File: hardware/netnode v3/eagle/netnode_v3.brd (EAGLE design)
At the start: 59.9 x 58.9 mm, 25 parts, among them IC1 TSR-1, IC2 PIC18F4K80, X1 DC10R, X2 XPORT

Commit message: Pre-final board files, silkscreen to be fixed
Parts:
- removed C5: 100n, rcl:C0603
- removed JP1: (no value), pinhead:1X06
- removed RST: 9902031, netnode:PUSHBUTTON
- removed UART: (no value), pinhead:1X04
- added ANALOG: (no value), pinhead:1X06
- added IC3: FOD060L, ic:SO-08
- added R1: 2K, rcl:R0603
- added R2: (no value), rcl:M0805
- added UART2: (no value), pinhead:1X04
- moved IO1 52.2 mm to (8.89, 5.08), turned to 0 degrees
- moved IO2 49.5 mm to (52.1, 5.08)
- moved X1 45.6 mm to (6.35, 53.3), turned to 270 degrees
- moved X2 38.8 mm to (16.5, 53.3), turned to 270 degrees
- moved SUP 36.1 mm to (2.54, 39.4), turned to 270 degrees
- moved HBEAT 24.3 mm to (14.0, 10.2), turned to 270 degrees
- moved XPORT 20.1 mm to (14.0, 14.0), turned to 270 degrees
- moved IC1 19.4 mm to (5.08, 26.7), turned to 0 degrees
- moved C1 19.1 mm to (13.8, 37.1), turned to 180 degrees
- moved C6 19.1 mm to (49.5, 38.1), turned to 0 degrees
- moved RN3 18.3 mm to (10.5, 22.9), turned to 0 degrees
- moved C7 18.2 mm to (34.3, 38.1), turned to 270 degrees
- moved PWR 17.3 mm to (14.0, 17.8), turned to 270 degrees
- moved RN1 16.2 mm to (44.5, 12.7)
- moved C2 15.9 mm to (13.8, 33.8), turned to 180 degrees
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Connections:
- removed net N$12: IC2.2, UART.2
- removed net N$9: HBEAT.C, IC2.15
- new net HBEAT: HBEAT.C, IC2.40
- new net N$3: IO1.1, R2.2
- new net OPTO1: IC2.41, IC3.6, R1.1
- new net RD4: IC2.2, UART2.2
- net !MCLR: no longer RST.3
- net +3V3: now also IC3.8, IO1.8, IO2.5, IO2.6, R1.2, RN3.6; no longer C5.1, IO1.1, RN3.5
- net AN0: now also ANALOG.1; no longer JP1.1
- net AN1: now also ANALOG.2; no longer JP1.2
- net AN2: now also ANALOG.4; no longer JP1.4
- net AN3: now also ANALOG.5; no longer JP1.5
- net GND: now also ANALOG.3, ANALOG.6, IC3.5, IO1.7, IO2.7, UART2.1; no longer C5.2, IO1.2, IO2.2, IO2.4, IO2.6, JP1.3, JP1.6, RST.1, UART.1
- net IN0: now also IO2.4, RN1.5; no longer IO2.1, RN1.8
- net IN1: now also RN1.6; no longer RN1.7
- net IN2: now also IO2.2, RN1.7; no longer IO2.5, RN1.6
- net IN3: now also IO2.1, RN1.8; no longer IO2.7, RN1.5
- net N$2: now also RN3.3; no longer RN3.1
- net N$8: now also RN3.1; no longer RN3.4
- net OPTO+: now also IC3.2, R2.1; no longer IO1.5
- net OPTO-: now also IC3.3, IO1.2; no longer IO1.6
- net OW: now also IO1.5; no longer IO1.7
- net PIC_RTS: now also IC2.35
- net PWM: now also IO1.6; no longer IO1.8
- net RX2: now also UART2.4; no longer UART.4
- net TX2: now also UART2.3; no longer UART.3
- net XPORT_RST: now also IC2.36
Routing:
- net +3V3: track 11.9 -> 241.2 mm, vias 0 -> 4
- net OPTO1: track 0.00 -> 59.2 mm, vias 0 -> 2
- net HBEAT: track 0.00 -> 45.5 mm, vias 0 -> 2
- net SCL: track 0.00 -> 41.0 mm, vias 0 -> 1
- net OW: track 0.00 -> 40.1 mm, vias 0 -> 1
- net SDA: track 0.00 -> 38.6 mm, vias 0 -> 1
- net PWM: track 0.00 -> 33.5 mm, vias 0 -> 1
- net XPORT_STAT: track 0.00 -> 32.1 mm, vias 0 -> 2
- net IN3: track 0.00 -> 27.8 mm, vias 0 -> 2
- net IN0: track 0.00 -> 26.8 mm, vias 0 -> 2
- net XPORT_RST: track 0.00 -> 25.5 mm, vias 0 -> 1
- net IN2: track 0.00 -> 23.8 mm, vias 0 -> 2
- net IN1: track 0.00 -> 22.5 mm
- net VSUPPLY: track 0.00 -> 21.5 mm
- net AN0: track 0.00 -> 20.1 mm, vias 0 -> 1
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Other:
- board size 59.9 x 58.9 mm -> 59.9 x 49.9 mm
- board text added: "0"
- board text added: "1"
- board text added: "2"
- board text added: "3"

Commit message: Further finalization of board
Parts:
- moved IO1 17.8 mm to (26.7, 5.08), turned to 180 degrees
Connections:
- net +3V3: now also IO1.1; no longer IO1.8
- net GND: now also IO1.2; no longer IO1.7
- net N$3: now also IO1.8; no longer IO1.1
- net OPTO-: now also IO1.7; no longer IO1.2
- net OW: now also IO1.4; no longer IO1.5
- net PWM: now also IO1.3; no longer IO1.6
- net SCL: now also IO1.6; no longer IO1.3
- net SDA: now also IO1.5; no longer IO1.4
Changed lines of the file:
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@@
 <setting verticaltext="up"/>
 </settings>
-<grid distance="1" unitdist="mm" unit="mm" style="lines" multiple="1" display="no" altdistance="0.127" altunitdist="mm" altunit="mm"/>
+<grid distance="2.54" unitdist="mm" unit="mm" style="lines" multiple="1" display="no" altdistance="0.127" altunitdist="mm" altunit="mm"/>
 <layers>
 <layer number="1" name="Top" color="4" fill="1" visible="yes" active="yes"/>
@@
 <layer number="27" name="tValues" color="7" fill="1" visible="no" active="yes"/>
 <layer number="28" name="bValues" color="7" fill="1" visible="no" active="yes"/>
-<layer number="29" name="tStop" color="7" fill="3" visible="yes" active="yes"/>
+<layer number="29" name="tStop" color="7" fill="3" visible="no" active="yes"/>
 <layer number="30" name="bStop" color="7" fill="6" visible="no" active="yes"/>
 <layer number="31" name="tCream" color="7" fill="4" visible="no" active="yes"/>
@@
 <attribute name="VALUE" x="14.639" y="36.066" size="1.27" layer="27" rot="R180"/>
 </element>
-<element name="IO1" library="netnode" package="SCREW_TERMINAL_8PINS" value="SCREW_TERMINAL" x="8.89" y="5.08">
-<attribute name="OC_FARNELL" value="3041438" x="8.89" y="5.08" size="1.778" layer="27" display="off"/>
-<attribute name="MF" value="PHOENIX CONTACT" x="8.89" y="5.08" size="1.778" layer="27" display="off"/>
-<attribute name="MPN" value="1725711" x="8.89" y="5.08" size="1.778" layer="27" display="off"/>
+<element name="IO1" library="netnode" package="SCREW_TERMINAL_8PINS" value="SCREW_TERMINAL" x="26.67" y="5.08" rot="R180">
+<attribute name="OC_FARNELL" value="3041438" x="26.67" y="5.08" size="1.778" layer="27" rot="R180" display="off"/>
+<attribute name="MF" value="PHOENIX CONTACT" x="26.67" y="5.08" size="1.778" layer="27" rot="R180" display="off"/>
+<attribute name="MPN" value="1725711" x="26.67" y="5.08" size="1.778" layer="27" rot="R180" display="off"/>
 </element>
 <element name="IO2" library="netnode" package="SCREW_TERMINAL_8PINS" value="SCREW_TERMINAL" x="52.07" y="5.08" rot="R180">
@@
 <contactref element="IC3" pad="5"/>
 <contactref element="IC3" pad="5"/>
-<contactref element="IO1" pad="7"/>
 <wire x1="44.12" y1="23.5" x2="44.12" y2="20.84" width="0.4064" layer="1"/>
 <wire x1="44.12" y1="20.84" x2="43.6" y2="20.32" width="0.4064" layer="1"/>
@@
 <via x="47.371" y="19.558" extent="1-16" drill="0.5"/>
 <via x="47.371" y="17.526" extent="1-16" drill="0.5"/>
+<contactref element="IO1" pad="2"/>
 </signal>
 <signal name="VSUPPLY" class="1">
@@
 <contactref element="IO2" pad="6"/>
 <contactref element="R1" pad="2"/>
-<contactref element="IO1" pad="8"/>
 <wire x1="44.92" y1="23.5" x2="44.92" y2="20.7" width="0.4064" layer="1"/>
 <wire x1="44.92" y1="20.7" x2="45.3" y2="20.32" width="0.4064" layer="1"/>
@@
 <wire x1="2.54" y1="10.16" x2="10.16" y2="2.54" width="1.016" layer="16" curve="90"/>
 <wire x1="10.16" y1="2.54" x2="26.67" y2="2.54" width="1.016" layer="16"/>
-<wire x1="26.67" y1="2.54" x2="39.37" y2="2.54" width="1.016" layer="16"/>
+<wire x1="27.94" y1="2.54" x2="39.37" y2="2.54" width="1.016" layer="16"/>
 <wire x1="39.37" y1="2.54" x2="41.91" y2="5.08" width="1.016" layer="16" curve="90"/>
 <wire x1="41.91" y1="5.08" x2="41.91" y2="9.84" width="0.4064" layer="1"/>
@@
 <wire x1="43.18" y1="7.62" x2="41.91" y2="6.35" width="0.4064" layer="16" curve="90"/>
 <wire x1="41.91" y1="6.35" x2="41.91" y2="5.08" width="0.4064" layer="16"/>
-<wire x1="26.67" y1="5.08" x2="26.67" y2="2.54" width="1.016" layer="16"/>
 <wire x1="39.37" y1="5.08" x2="41.91" y2="5.08" width="1.016" layer="16"/>
 <wire x1="55.746" y1="20.38" x2="55.94" y2="20.38" width="0.4064" layer="1"/>
@@
 <via x="40.64" y="41.91" extent="1-16" drill="0.5"/>
 <via x="41.91" y="41.91" extent="1-16" drill="0.5"/>
+<contactref element="IO1" pad="1"/>
+<wire x1="26.67" y1="5.08" x2="26.67" y2="2.54" width="1.016" layer="16"/>
+<wire x1="26.67" y1="2.54" x2="27.94" y2="2.54" width="1.016" layer="16"/>
 </signal>
 <signal name="XPORT_RST">
@@
 </signal>
 <signal name="SCL" class="1">
-<contactref element="IO1" pad="3"/>
 <contactref element="IC2" pad="37"/>
-<wire x1="13.97" y1="5.08" x2="13.97" y2="6.35" width="0.4064" layer="16"/>
 <wire x1="13.97" y1="6.35" x2="24.13" y2="16.51" width="0.4064" layer="16"/>
 <wire x1="24.13" y1="16.51" x2="31.75" y2="16.51" width="0.4064" layer="16"/>
@@
 <wire x1="33.02" y1="26.67" x2="37.25" y2="30.9" width="0.4064" layer="1"/>
 <wire x1="38.32" y1="30.9" x2="37.25" y2="30.9" width="0.4064" layer="1"/>
+<contactref element="IO1" pad="6"/>
+<wire x1="13.97" y1="6.35" x2="13.97" y2="5.08" width="0.4064" layer="16"/>
 </signal>
 <signal name="SDA" class="1">
-<contactref element="IO1" pad="4"/>
 <contactref element="IC2" pad="42"/>
-<wire x1="16.51" y1="5.08" x2="16.51" y2="6.35" width="0.4064" layer="16"/>
 <wire x1="16.51" y1="6.35" x2="24.13" y2="13.97" width="0.4064" layer="16"/>
 <wire x1="24.13" y1="13.97" x2="33.02" y2="13.97" width="0.4064" layer="16"/>
@@
 <wire x1="35.56" y1="20.32" x2="35.56" y2="16.51" width="0.4064" layer="16"/>
 <wire x1="35.56" y1="16.51" x2="33.02" y2="13.97" width="0.4064" layer="16"/>
+<contactref element="IO1" pad="5"/>
+<wire x1="16.51" y1="6.35" x2="16.51" y2="5.08" width="0.4064" layer="16"/>
 </signal>
 <signal name="OPTO+" class="1">
@@
 <signal name="OPTO-" class="1">
 <contactref element="IC3" pad="3"/>
-<contactref element="IO1" pad="2"/>
 <wire x1="5.715" y1="13.91" x2="5.715" y2="9.525" width="0.4064" layer="1"/>
 <wire x1="5.715" y1="9.525" x2="7.62" y2="7.62" width="0.4064" layer="1"/>
 <wire x1="7.62" y1="7.62" x2="10.16" y2="7.62" width="0.4064" layer="1"/>
 <wire x1="10.16" y1="7.62" x2="11.43" y2="6.35" width="0.4064" layer="1"/>
+<contactref element="IO1" pad="7"/>
 <wire x1="11.43" y1="6.35" x2="11.43" y2="5.08" width="0.4064" layer="1"/>
 </signal>
 <signal name="OW" class="1">
 <contactref element="IC2" pad="43"/>
-<contactref element="IO1" pad="5"/>
 <wire x1="38.32" y1="26.1" x2="40.64" y2="26.1" width="0.4064" layer="1"/>
 <wire x1="40.64" y1="26.1" x2="40.64" y2="26.67" width="0.4064" layer="1"/>
@@
 <wire x1="35.56" y1="11.43" x2="24.13" y2="11.43" width="0.4064" layer="16"/>
 <wire x1="24.13" y1="11.43" x2="19.05" y2="6.35" width="0.4064" layer="16"/>
+<contactref element="IO1" pad="4"/>
 <wire x1="19.05" y1="6.35" x2="19.05" y2="5.08" width="0.4064" layer="16"/>
 </signal>
 <signal name="PWM" class="1">
 <contactref element="IC2" pad="3"/>
-<contactref element="IO1" pad="6"/>
 <wire x1="41.72" y1="23.5" x2="41.72" y2="21.4" width="0.4064" layer="1"/>
 <wire x1="41.72" y1="21.4" x2="40.64" y2="20.32" width="0.4064" layer="1"/>
@@
 <wire x1="35.56" y1="8.89" x2="24.13" y2="8.89" width="0.4064" layer="16"/>
 <wire x1="24.13" y1="8.89" x2="21.59" y2="6.35" width="0.4064" layer="16"/>
+<contactref element="IO1" pad="3"/>
 <wire x1="21.59" y1="6.35" x2="21.59" y2="5.08" width="0.4064" layer="16"/>
 </signal>
@@
 <via x="19.05" y="16.51" extent="1-16" drill="0.5"/>
 </signal>
-<signal name="N$3">
-<contactref element="IO1" pad="1"/>
-<contactref element="R2" pad="2"/>
-<wire x1="8.89" y1="5.08" x2="5.08" y2="5.08" width="0.4064" layer="1"/>
-<wire x1="5.08" y1="5.08" x2="3.81" y2="6.35" width="0.4064" layer="1"/>
-<wire x1="3.81" y1="6.35" x2="3.81" y2="6.67" width="0.4064" layer="1"/>
-</signal>
 <signal name="N$2">
 <contactref element="PWR" pad="A"/>
@@
 <wire x1="11.43" y1="17.78" x2="12.22" y2="17.78" width="0.4064" layer="1"/>
 </signal>
+<signal name="N$3">
+<contactref element="IO1" pad="8"/>
+<contactref element="R2" pad="2"/>
+<wire x1="3.81" y1="6.67" x2="5.4" y2="5.08" width="0.4064" layer="1" curve="90"/>
+<wire x1="5.4" y1="5.08" x2="8.89" y2="5.08" width="0.4064" layer="1"/>
+</signal>
 </signals>

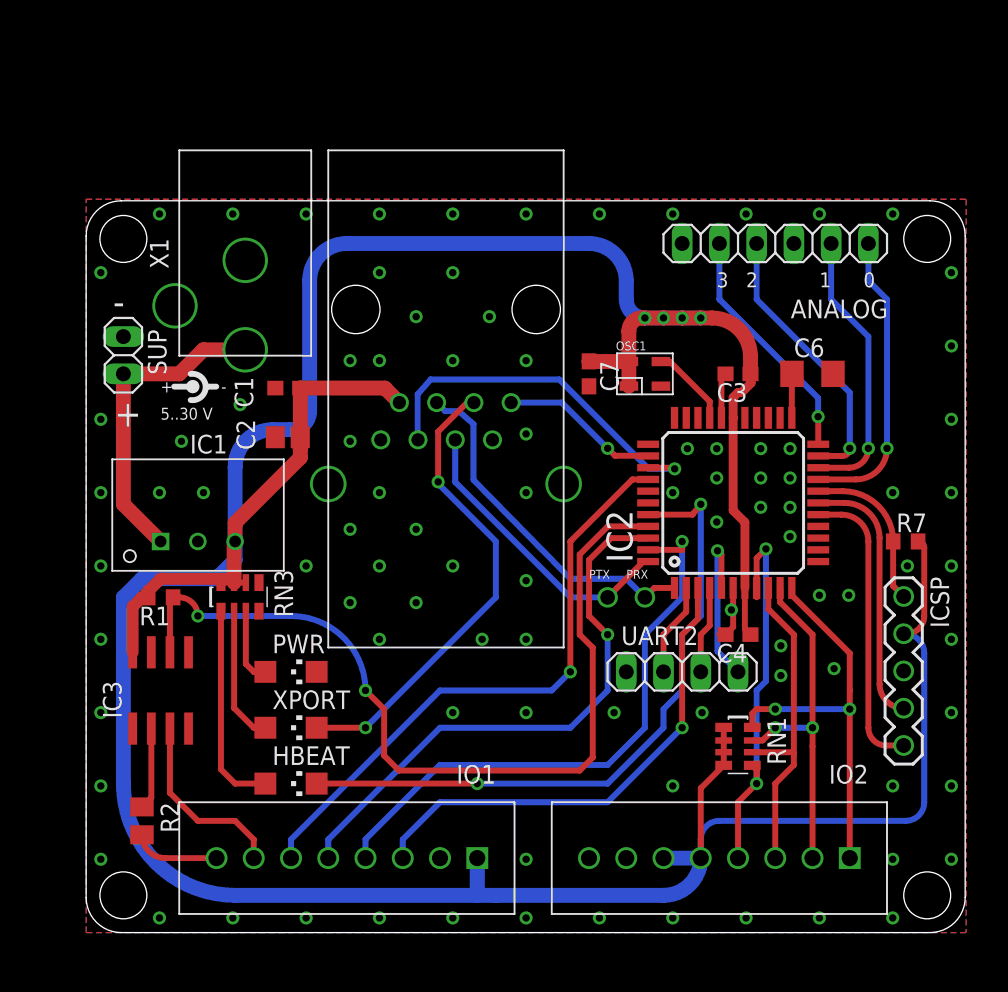
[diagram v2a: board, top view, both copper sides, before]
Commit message: Added resistors and cleaned silkscreen
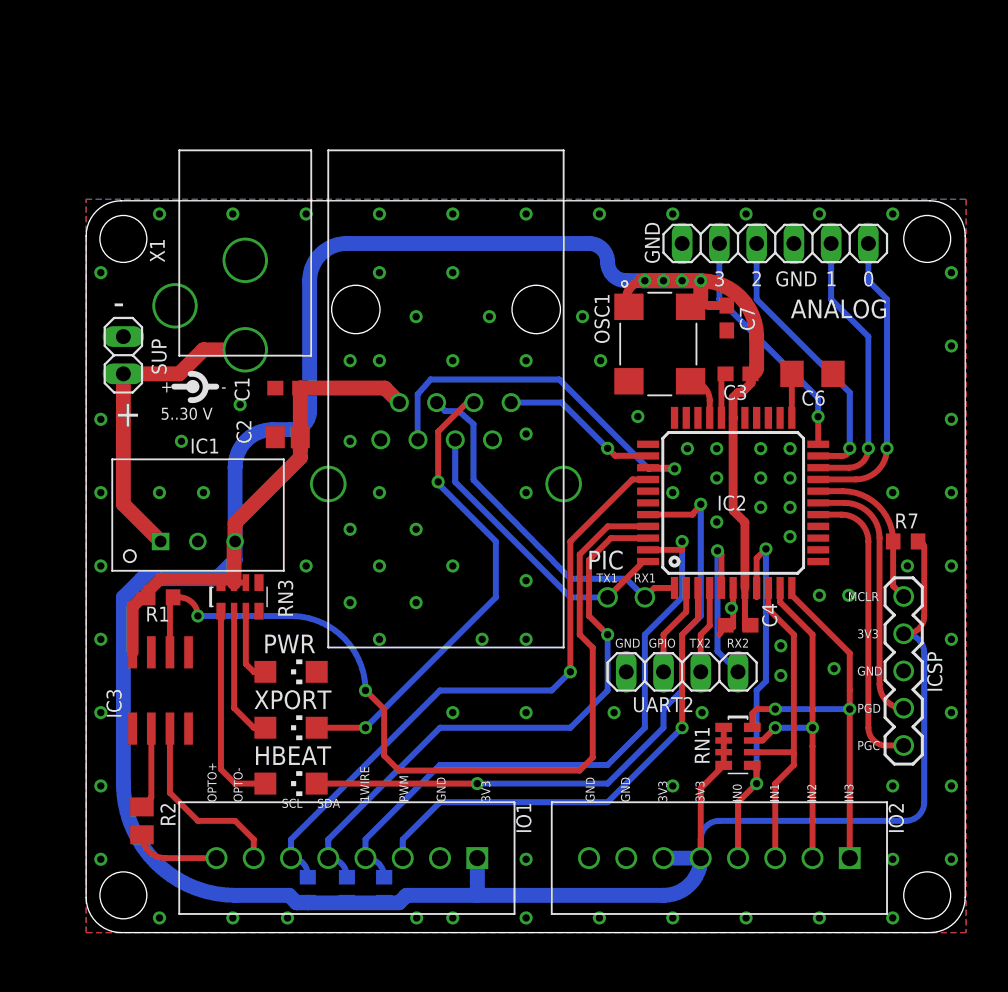
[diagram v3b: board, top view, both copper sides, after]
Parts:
- added R3, R4, R5: (no value), rcl:R0603
- OSC1: device mbed:OSC3.2X.2.5 -> passives:7W_7X5
- moved C7 10.1 mm to (43.7, 41.9)
- moved OSC1 2.27 mm to (39.1, 40.1), turned to 270 degrees
- moved C4 0.63 mm to (44.5, 21.0)
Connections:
- net N$3 renamed OPTO+_PRE_RES
- net +3V3: now also OSC1.1, OSC1.4, R3.2, R4.2, R5.2; no longer OSC1.P$1, OSC1.P$4
- net 12MHZ: now also OSC1.3; no longer OSC1.P$3
- net GND: now also OSC1.2; no longer OSC1.P$2
- net OW: now also R3.1
- net SCL: now also R5.1
- net SDA: now also R4.1
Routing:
- net +3V3: track 241.2 -> 245.0 mm
- net 12MHZ: track 5.57 -> 3.03 mm
- net SDA: track 38.6 -> 40.4 mm
- net OW: track 40.1 -> 42.0 mm
- net SCL: track 41.0 -> 42.8 mm
- net GND: track 6.93 -> 7.07 mm, vias 94 -> 97
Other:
- board text added: "1WIRE"
- board text added: "3V3"
- board text added: "GND"
- board text added: "GPIO"
- board text added: "IN0"
- board text added: "IN1"
- board text added: "IN2"
- board text added: "IN3"
- board text added: "MCLR"
- board text added: "OPTO+"
- board text added: "OPTO-"
- board text added: "PGC"
- board text added: "PGD"
- board text added: "PIC"
- board text added: "PWM"
- board text added: "RX1"
- board text added: "RX2"
- board text added: "SCL"
- board text added: "SDA"
- board text added: "TX1"
- board text added: "TX2"
- board text removed: "PRX"
- board text removed: "PTX"

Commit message: Further board cleanup
* Silkscreen fixes + size increased
* Replaced 0603 componentsn with 0805 counterparts for easier soldering
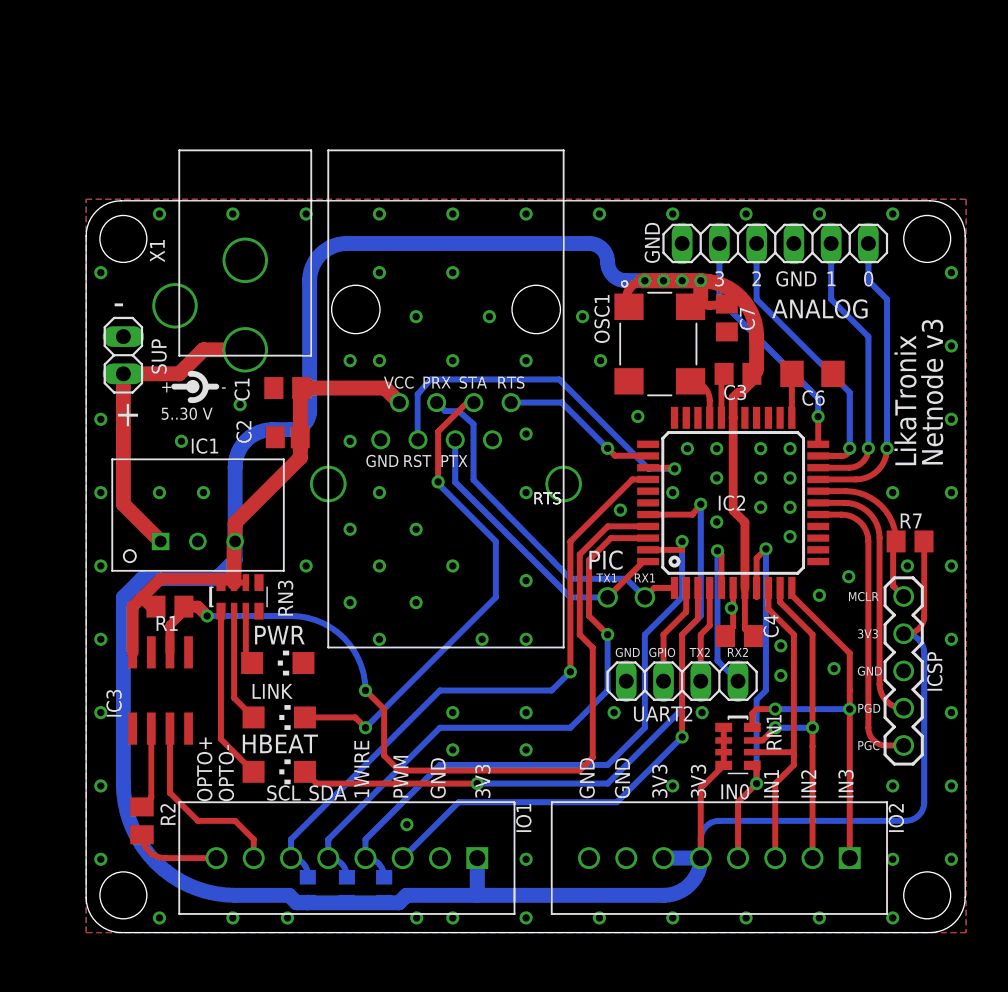
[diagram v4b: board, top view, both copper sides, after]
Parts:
- removed XPORT: (no value), led:CHIPLED_1206
- added LINK: (no value), led:CHIPLED_1206
- C1, C7: device netnode:C0603 -> rcl:C0805
- C3, C4: device rcl:C0603 -> rcl:C0805
- R1, R7: device rcl:R0603 -> rcl:R0805
- moved HBEAT 1.13 mm to (13.2, 11.0)
- moved PWR 1.08 mm to (13.1, 18.4)
- moved R1 0.90 mm to (5.71, 22.2)
- moved C4 0.74 mm to (44.5, 20.2)
- moved UART2 0.64 mm to (40.6, 17.1)
- moved R7 0.30 mm to (56.2, 26.7)
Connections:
- net N$1: now also LINK.A; no longer XPORT.A
- net XPORT_STAT: now also LINK.C; no longer XPORT.C
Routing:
- net N$8: track 14.2 -> 11.9 mm
- net N$1: track 9.29 -> 7.80 mm
- net N$2: track 5.15 -> 3.71 mm
- net OPTO1: track 59.2 -> 57.9 mm
- net HBEAT: track 45.5 -> 46.6 mm
- net XPORT_STAT: track 32.1 -> 33.2 mm
- net +3V3: track 245.0 -> 246.1 mm
- net TX2: track 5.97 -> 6.61 mm
- net RD4: track 6.36 -> 7.00 mm
- net RX2: track 11.5 -> 12.1 mm
- net GND: track 7.07 -> 6.95 mm, vias 97 -> 101
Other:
- board text added: "LikaTronix"
- board text added: "Netnode v3"
- board text added: "PRX"
- board text added: "PTX"
- board text added: "RST"
- board text added: "RTS"
- board text added: "STA"
- board text added: "VCC"
